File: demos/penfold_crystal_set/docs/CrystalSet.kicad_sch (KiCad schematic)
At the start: 6 parts

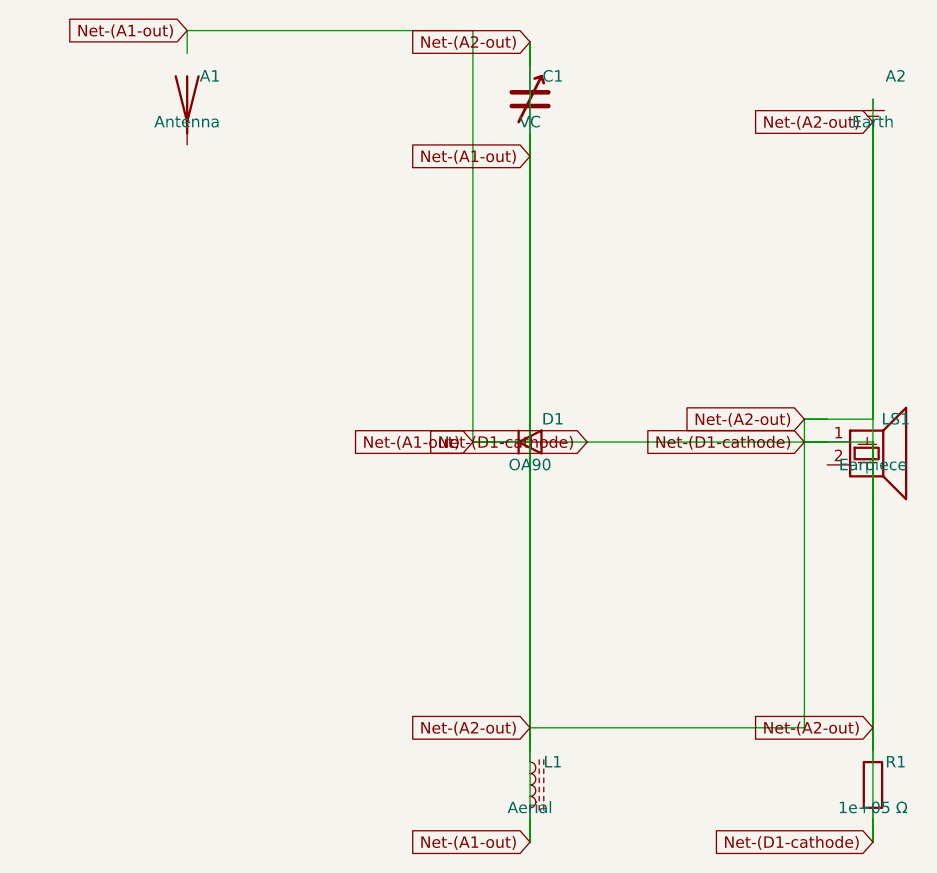
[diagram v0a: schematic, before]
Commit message: catalogue: Penfold corpus remediation — six well-bounded defect fixes
Closes the six findings from the catalogue review (.plans/penfold-corpus-remediation-spec.md):

  1. VariableCapacitor footprint was a polarised electrolytic
     (Capacitor_THT:CP_Radial_*) — replaced with
     Connector:Conn_01x02_Pin to model the breadboard-side
     flying-lead connection; LAYOUT.kind = 'off_board_flying_lead'.

  2. FerriteAerial footprint was a small radial inductor
     (Inductor_THT:L_Radial_*) — same Connector fix; the actual
     50–100 mm rod lives off-board in a clip.

  3. CrystalEarpiece REFDES_PREFIX changed from 'LS' to 'BZ' so it
     doesn't collide with Speaker's 'LS' in any future Circuit that
     composes both; footprint changed from Buzzer_Beeper:* to
     Connector_Audio:Jack_3.5mm_*.

  4. Earth REFDES_PREFIX changed from 'A' to 'E' so it doesn't
     collide with Antenna's 'A' in any future implicit-numbering
     design.  Crystal Set demo's Earth now constructs at
     refdes_number=1 (its own number-space) rather than =2.

  5. Antenna gains DRIVE_BEHAVIOUR = 'environment_fed' ClassVar +
     clarifying comment naming the informational-OUT-marker contract
     for downstream consumers (validate CLI, net-report, SPICE).

  6. Every concrete Diode subclass now declares V_F: ClassVar[float]
     and V_BREAKDOWN_R: ClassVar[float | None] for cross-family
     consistency.  Zeners carry their breakdown voltage in
     V_BREAKDOWN_R (3.3 V, 5.1 V, 12.0 V); non-Zener diodes set it
     to None.  Schottky 1N5817 declares V_F = 0.32; silicon diodes
     declare 0.7; the existing germanium D_OA90 already declared 0.2.

framework: IEEE_315_PREFIXES grows two entries — 'BZ' (buzzer / piezo
earpiece) and 'E' (earth-ground) — to admit the new refdes prefixes.

kicad_sch: symbol_map updated so CrystalEarpiece resolves with the 'BZ'
prefix and Earth with 'E'; everything else mechanical follows.

tests: 31 new targeted regression tests across three modules
(off_board_la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
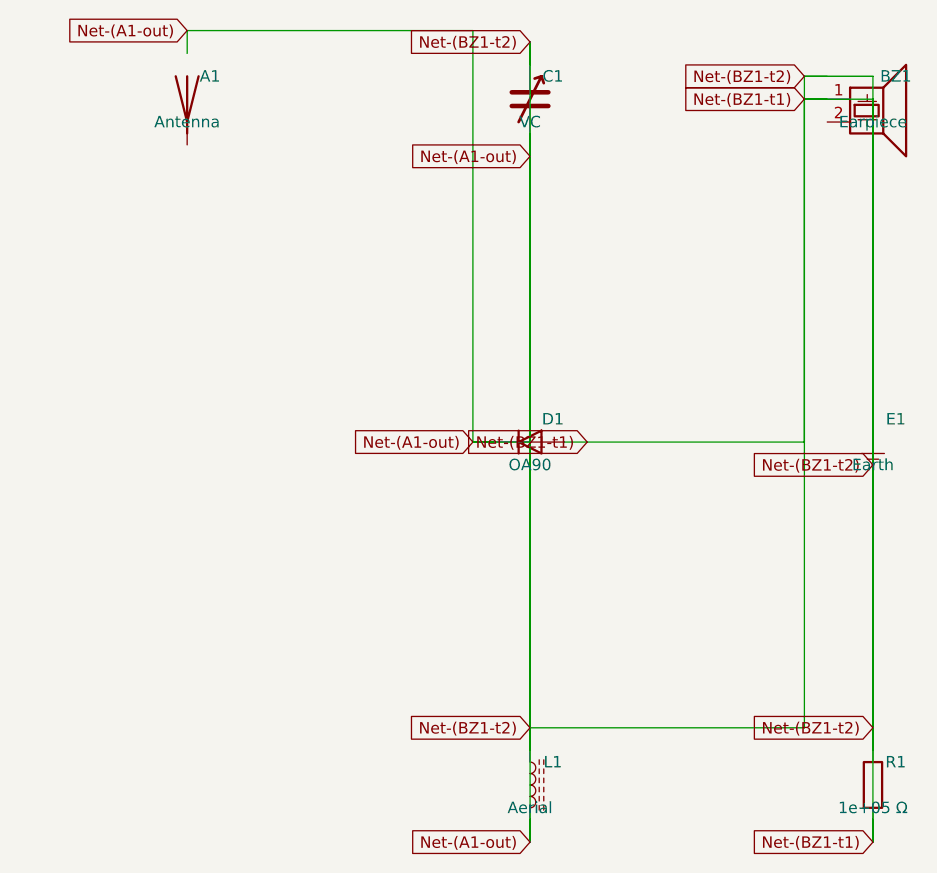
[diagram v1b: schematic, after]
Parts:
- removed LS1: Earpiece, symbol Device:Speaker_Crystal
- added BZ1: Earpiece, symbol Device:Speaker_Crystal
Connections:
- net Earth: now also BZ1.1
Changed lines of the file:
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@@
   (symbol
     (lib_id "power:Earth")
-    (at 101.6 25.4 0)
-    (unit 1)
-    (exclude_from_sim no)
-    (in_bom yes)
-    (on_board yes)
-    (dnp no)
-    (property "Reference" "A2"
-      (at 104.14 22.86 0)
+    (at 101.6 63.5 0)
+    (unit 1)
+    (exclude_from_sim no)
+    (in_bom yes)
+    (on_board yes)
+    (dnp no)
+    (property "Reference" "E1"
+      (at 104.14 60.96 0)
       (effects (font (size 1.27 1.27)))
     )
     (property "Value" "Earth"
-      (at 101.6 27.94 0)
-      (effects (font (size 1.27 1.27)))
-    )
-    (pin "1")
-  )
-  (wire
-    (pts (xy 101.6 25.4) (xy 101.6 27.94))
-    (stroke (width 0) (type default))
-  )
-  (global_label "Net-(A2-out)"
-    (shape input)
-    (at 101.6 27.94 0)
+      (at 101.6 66.04 0)
+      (effects (font (size 1.27 1.27)))
+    )
+    (pin "1")
+  )
+  (wire
+    (pts (xy 101.6 63.5) (xy 101.6 66.04))
+    (stroke (width 0) (type default))
+  )
+  (global_label "Net-(BZ1-t2)"
+    (shape input)
+    (at 101.6 66.04 0)
     (fields_autoplaced yes)
     (effects (font (size 1.27 1.27)) (justify right))
@@
     (stroke (width 0) (type default))
   )
-  (global_label "Net-(A2-out)"
+  (global_label "Net-(BZ1-t2)"
     (shape input)
     (at 63.5 95.25 0)
@@
     (stroke (width 0) (type default))
   )
-  (global_label "Net-(A2-out)"
+  (global_label "Net-(BZ1-t2)"
     (shape input)
     (at 63.5 19.05 0)
@@
     (stroke (width 0) (type default))
   )
-  (global_label "Net-(D1-cathode)"
+  (global_label "Net-(BZ1-t1)"
     (shape input)
     (at 69.85 63.5 0)
@@
     (stroke (width 0) (type default))
   )
-  (global_label "Net-(D1-cathode)"
+  (global_label "Net-(BZ1-t1)"
     (shape input)
     (at 101.6 107.95 0)
@@
     (stroke (width 0) (type default))
   )
-  (global_label "Net-(A2-out)"
+  (global_label "Net-(BZ1-t2)"
     (shape input)
     (at 101.6 95.25 0)
@@
   (symbol
     (lib_id "Device:Speaker_Crystal")
-    (at 101.6 63.5 0)
-    (unit 1)
-    (exclude_from_sim no)
-    (in_bom yes)
-    (on_board yes)
-    (dnp no)
-    (property "Reference" "LS1"
-      (at 104.14 60.96 0)
+    (at 101.6 25.4 0)
+    (unit 1)
+    (exclude_from_sim no)
+    (in_bom yes)
+    (on_board yes)
+    (dnp no)
+    (property "Reference" "BZ1"
+      (at 104.14 22.86 0)
       (effects (font (size 1.27 1.27)))
     )
     (property "Value" "Earpiece"
-      (at 101.6 66.04 0)
-      (effects (font (size 1.27 1.27)))
-    )
-    (pin "1")
-    (pin "2")
-  )
-  (wire
-    (pts (xy 96.52 63.5) (xy 93.98 63.5))
-    (stroke (width 0) (type default))
-  )
-  (global_label "Net-(D1-cathode)"
-    (shape input)
-    (at 93.98 63.5 0)
-    (fields_autoplaced yes)
-    (effects (font (size 1.27 1.27)) (justify right))
-    (property "Intersheet References" "${INTERSHEET_REFS}"
-      (at 0 0 0)
-      (effects (font (size 1.27 1.27)) (hide yes))
-    )
-  )
-  (wire
-    (pts (xy 96.52 60.96) (xy 93.98 60.96))
-    (stroke (width 0) (type default))
-  )
-  (global_label "Net-(A2-out)"
-    (shape input)
-    (at 93.98 60.96 0)
+      (at 101.6 27.94 0)
+      (effects (font (size 1.27 1.27)))
+    )
+    (pin "1")
+    (pin "2")
+  )
+  (wire
+    (pts (xy 96.52 25.4) (xy 93.98 25.4))
+    (stroke (width 0) (type default))
+  )
+  (global_label "Net-(BZ1-t1)"
+    (shape input)
+    (at 93.98 25.4 0)
+    (fields_autoplaced yes)
+    (effects (font (size 1.27 1.27)) (justify right))
+    (property "Intersheet References" "${INTERSHEET_REFS}"
+      (at 0 0 0)
+      (effects (font (size 1.27 1.27)) (hide yes))
+    )
+  )
+  (wire
+    (pts (xy 96.52 22.86) (xy 93.98 22.86))
+    (stroke (width 0) (type default))
+  )
+  (global_label "Net-(BZ1-t2)"
+    (shape input)
+    (at 93.98 22.86 0)
     (fields_autoplaced yes)
     (effects (font (size 1.27 1.27)) (justify right))
@@
   )
   (wire
+    (pts (xy 69.85 63.5) (xy 93.98 63.5))
+    (stroke (width 0) (type default))
+  )
+  (wire
+    (pts (xy 93.98 63.5) (xy 93.98 25.4))
+    (stroke (width 0) (type default))
+  )
+  (wire
+    (pts (xy 93.98 25.4) (xy 101.6 25.4))
+    (stroke (width 0) (type default))
+  )
+  (wire
+    (pts (xy 101.6 25.4) (xy 101.6 107.95))
+    (stroke (width 0) (type default))
+  )
+  (wire
     (pts (xy 63.5 19.05) (xy 63.5 95.25))
     (stroke (width 0) (type default))
@@
   )
   (wire
-    (pts (xy 93.98 95.25) (xy 93.98 60.96))
-    (stroke (width 0) (type default))
-  )
-  (wire
-    (pts (xy 93.98 60.96) (xy 101.6 60.96))
-    (stroke (width 0) (type default))
-  )
-  (wire
-    (pts (xy 101.6 60.96) (xy 101.6 27.94))
-    (stroke (width 0) (type default))
-  )
-  (wire
-    (pts (xy 101.6 27.94) (xy 101.6 95.25))
-    (stroke (width 0) (type default))
-  )
-  (wire
-    (pts (xy 69.85 63.5) (xy 93.98 63.5))
-    (stroke (width 0) (type default))
-  )
-  (wire
-    (pts (xy 93.98 63.5) (xy 101.6 63.5))
-    (stroke (width 0) (type default))
-  )
-  (wire
-    (pts (xy 101.6 63.5) (xy 101.6 107.95))
-    (stroke (width 0) (type default))
-  )
+    (pts (xy 93.98 95.25) (xy 93.98 22.86))
+    (stroke (width 0) (type default))
+  )
+  (wire
+    (pts (xy 93.98 22.86) (xy 101.6 22.86))
+    (stroke (width 0) (type default))
+  )
+  (wire
+    (pts (xy 101.6 22.86) (xy 101.6 66.04))
+    (stroke (width 0) (type default))
+  )
+  (wire
+    (pts (xy 101.6 66.04) (xy 101.6 95.25))
+    (stroke (width 0) (type default))
+  )
